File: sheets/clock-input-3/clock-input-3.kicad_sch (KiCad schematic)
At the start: 14 parts, among them U1 40106

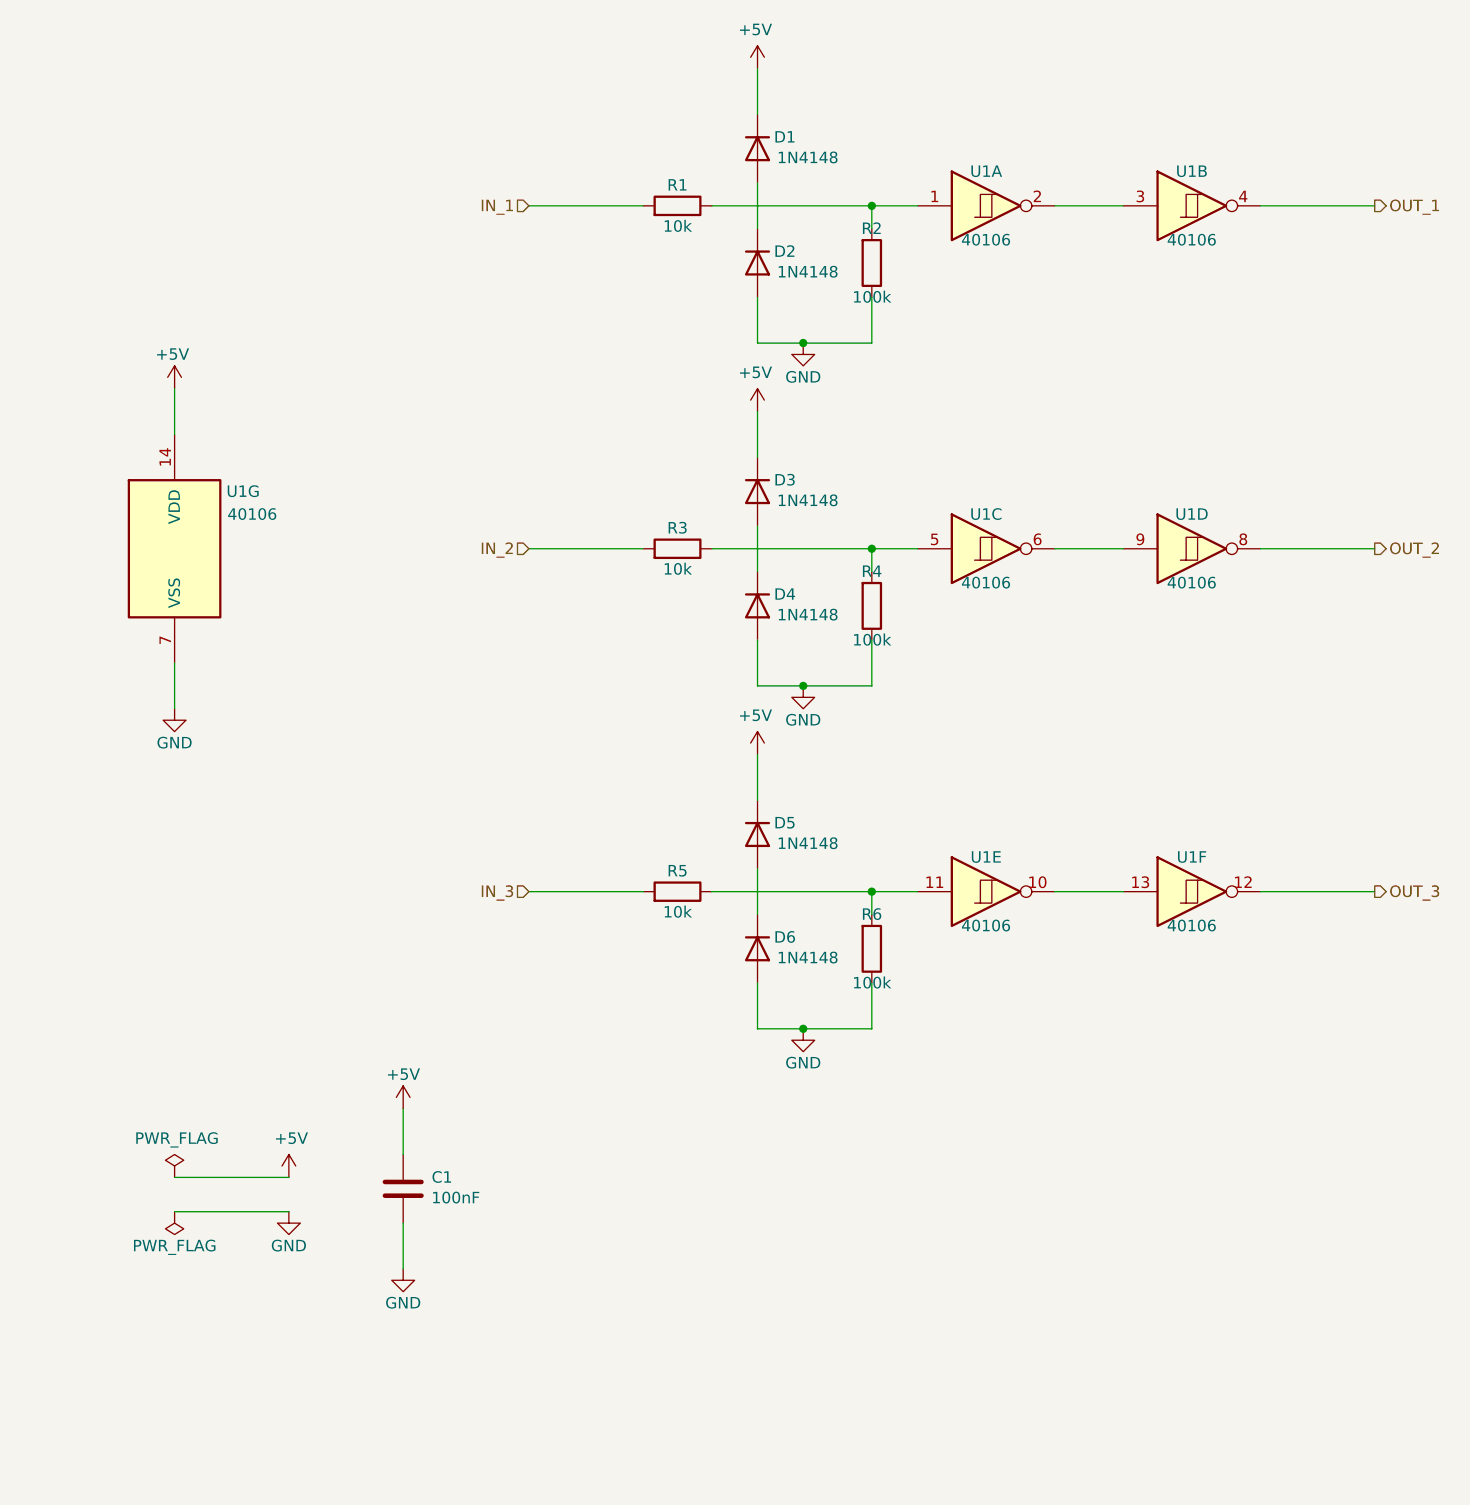
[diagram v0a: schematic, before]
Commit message: Restore clock-input-3's protection wiring
A KiCad save during the dowel-hole commits rewrote the sheet and left every
channel's clamp diodes on their own net, connected to nothing. Netlisted in a
module, channel 1 read

  D4.2, D5.1

where it must read

  D4.2, D5.1, R2.2, R3.1, U2.1

so the 1N4148 pair sat isolated instead of across the protected node. The block
exists to clamp a Eurorack-level input to CMOS levels, so this defeated its
whole purpose while ERC stayed clean.

Restored from 87cc8af, the last revision with the wiring intact: 72 junctions
and 36 wire segments, against 6 and 39 in the broken version. Verified by
netlisting the block inside step-sequencer-8 and comparing the clamp nets on all
three channels.

Also record what assembling a module taught us in docs/learnings.md.
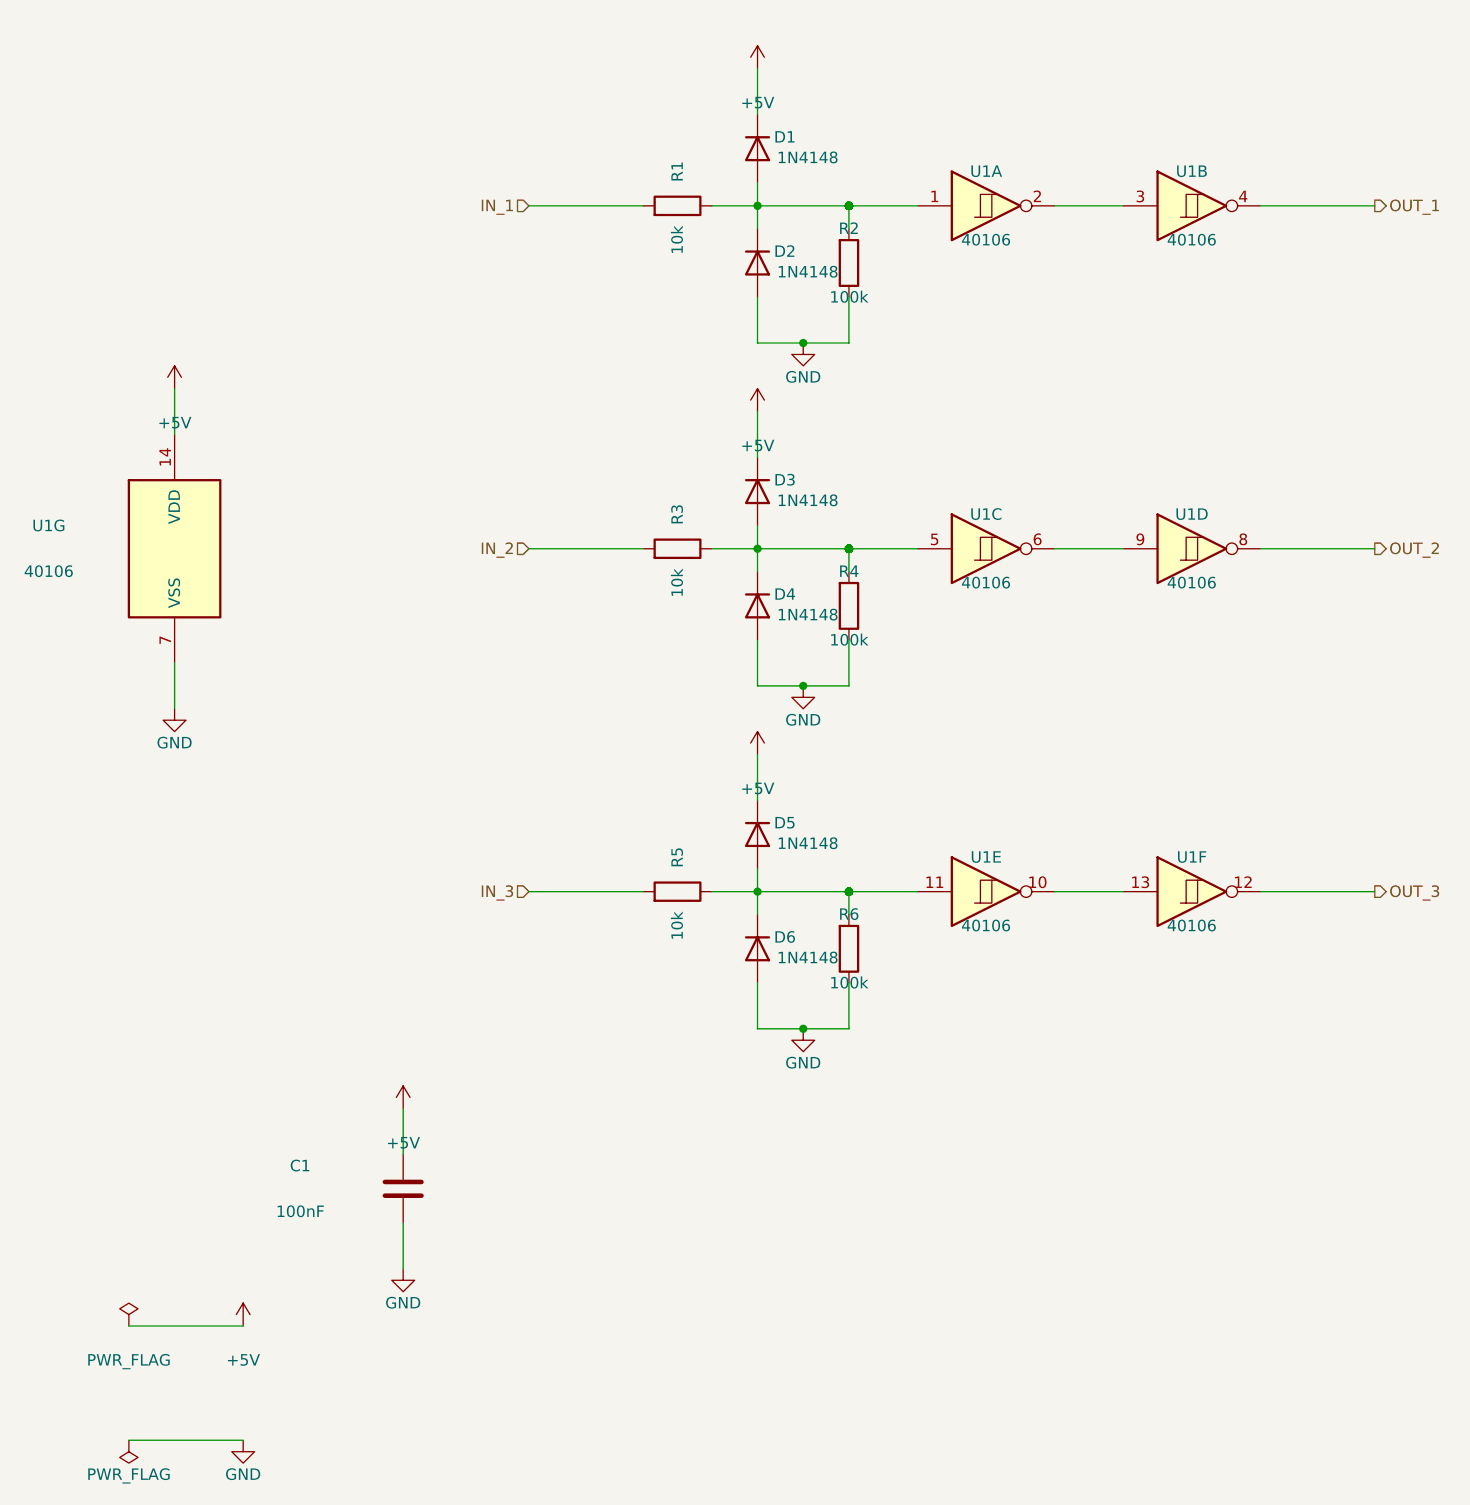
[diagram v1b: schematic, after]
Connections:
- net at R5.2, R6.1, U1.11: now also D5.2 (A), D6.1 (K)
- net at R3.2, R4.1, U1.5: now also D3.2 (A), D4.1 (K)
- net at D1.2 (A), D2.1 (K): now also R1.2, R2.1, U1.1
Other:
- moved on the sheet: R2, R4, R6
